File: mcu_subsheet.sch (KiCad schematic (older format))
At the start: 34 parts

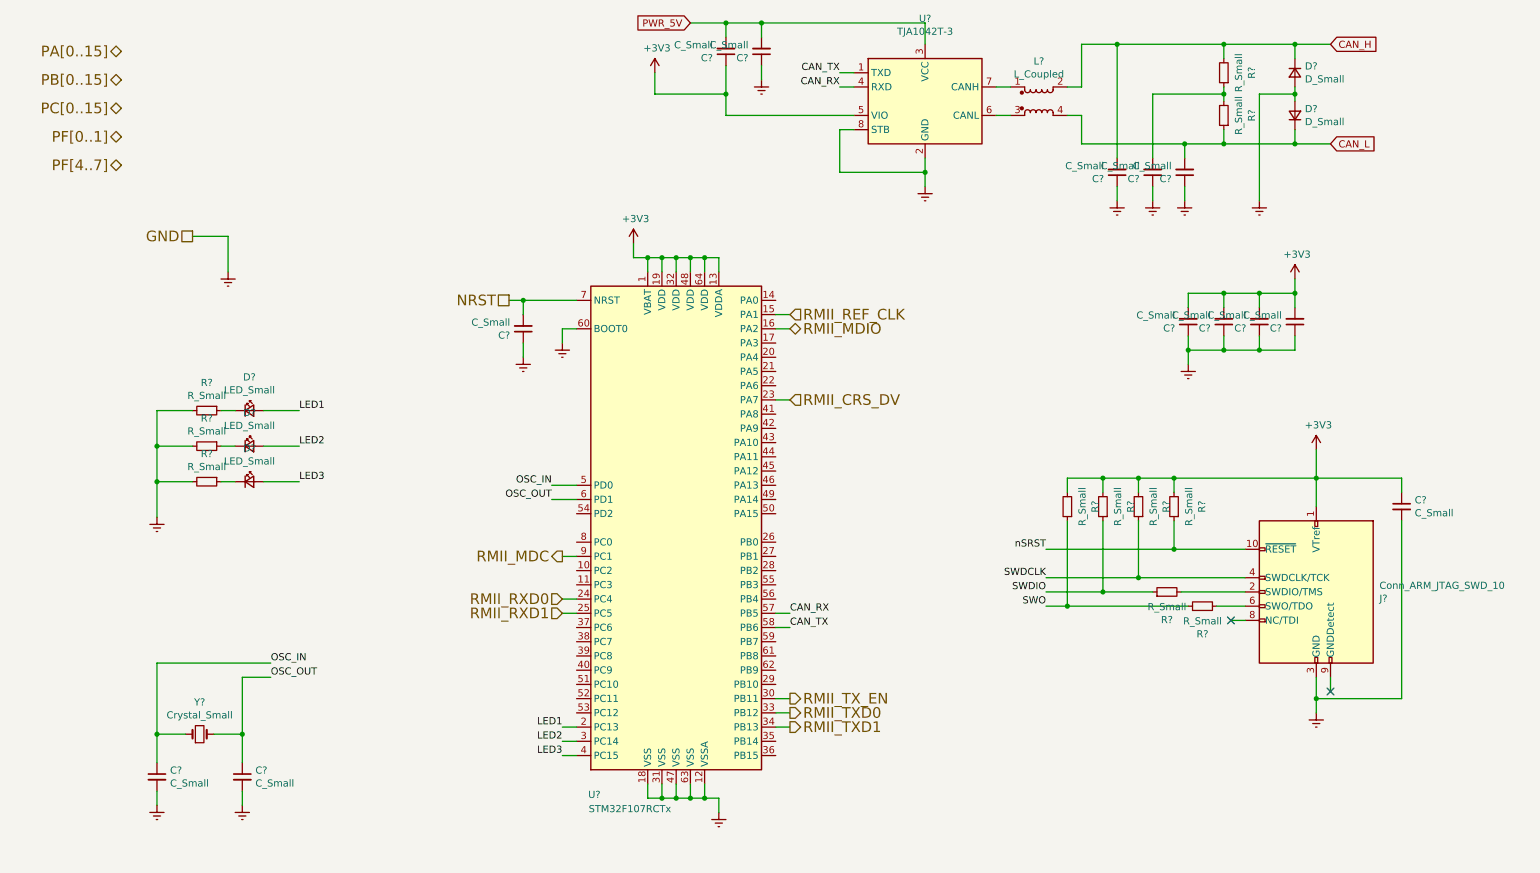
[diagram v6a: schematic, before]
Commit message: [can]:can lines protection + debug pinout connection
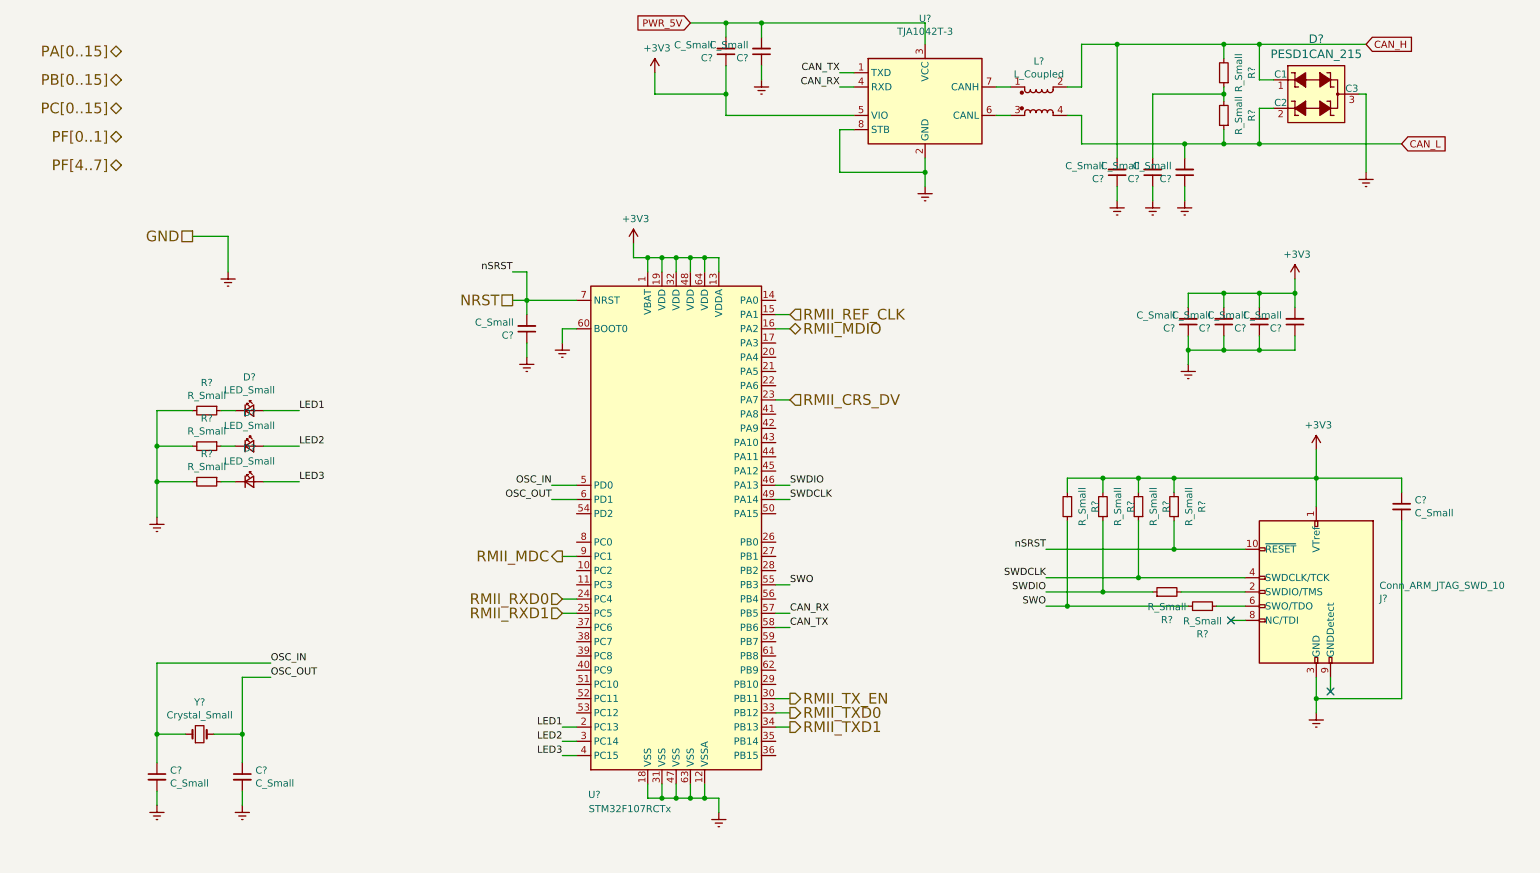
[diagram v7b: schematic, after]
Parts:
- removed D? (x2): D_Small, symbol Device:D_Small
- added D?: PESD1CAN_215, digikey-footprints:SOT-23-3, symbol dk_TVS-Diodes:PESD1CAN_215
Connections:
- net nSRST is gone; now on net NRST: J?.10 (~RESET~), R?.1
- net CAN_H: now also D?.1 (C1)
- net CAN_L: now also D?.2 (C2)
- net Earth: now also D?.3 (C3)
- net SWDCLK: now also U?.49 (PA14)
- net SWDIO: now also U?.46 (PA13)
- net SWO: now also U?.55 (PB3)
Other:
- moved on the sheet: C?
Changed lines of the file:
@@
 Text HLabel 2000 2500 0    75   UnSpc ~ 0
 GND
-Text HLabel 4225 2950 0    75   UnSpc ~ 0
+Text HLabel 4250 2950 0    75   UnSpc ~ 0
 NRST
 Text HLabel 1500 1200 0    75   BiDi ~ 0
@@
 L Device:C_Small C?
 U 1 1 61D7B19B
-P 4325 3150
-F 0 "C?" H 4417 3196 50  0000 L CNN
-F 1 "C_Small" H 4417 3105 50  0000 L CNN
-F 2 "" H 4325 3150 50  0001 C CNN
-F 3 "~" H 4325 3150 50  0001 C CNN
-	1    4325 3150
-	-1   0    0    1
-$EndComp
-Wire Wire Line
-	4325 3050 4325 2950
-Wire Wire Line
-	4325 2950 4700 2950
+P 4350 3150
+F 0 "C?" H 4442 3196 50  0000 L CNN
+F 1 "C_Small" H 4442 3105 50  0000 L CNN
+F 2 "" H 4350 3150 50  0001 C CNN
+F 3 "~" H 4350 3150 50  0001 C CNN
+	1    4350 3150
+	-1   0    0    1
+$EndComp
 $Comp
 L power:Earth #PWR?
 U 1 1 61D7EBFD
-P 4325 3350
-F 0 "#PWR?" H 4325 3100 50  0001 C CNN
-F 1 "Earth" H 4325 3200 50  0001 C CNN
-F 2 "" H 4325 3350 50  0001 C CNN
-F 3 "~" H 4325 3350 50  0001 C CNN
-	1    4325 3350
-	1    0    0    -1
-$EndComp
-Wire Wire Line
-	4325 3350 4325 3250
+P 4350 3350
+F 0 "#PWR?" H 4350 3100 50  0001 C CNN
+F 1 "Earth" H 4350 3200 50  0001 C CNN
+F 2 "" H 4350 3350 50  0001 C CNN
+F 3 "~" H 4350 3350 50  0001 C CNN
+	1    4350 3350
+	1    0    0    -1
+$EndComp
+Wire Wire Line
+	4350 3350 4350 3250
 $Comp
 L power:Earth #PWR?
@@
 Wire Wire Line
 	4600 3150 4600 3250
-Wire Wire Line
-	4225 2950 4325 2950
-Connection ~ 4325 2950
 $Comp
 L Device:Crystal_Small Y?
@@
 	1    0    0    -1
 $EndComp
-$Comp
-L Device:D_Small D?
-U 1 1 61E0E1EA
-P 9750 1350
-F 0 "D?" V 9704 1420 50  0000 L CNN
-F 1 "D_Small" V 9795 1420 50  0000 L CNN
-F 2 "" V 9750 1350 50  0001 C CNN
-F 3 "~" V 9750 1350 50  0001 C CNN
-	1    9750 1350
-	0    1    1    0
-$EndComp
-$Comp
-L Device:D_Small D?
-U 1 1 61E0EA92
-P 9750 1650
-F 0 "D?" V 9796 1580 50  0000 R CNN
-F 1 "D_Small" V 9705 1580 50  0000 R CNN
-F 2 "" V 9750 1650 50  0001 C CNN
-F 3 "~" V 9750 1650 50  0001 C CNN
-	1    9750 1650
-	0    -1   -1   0
-$EndComp
 Wire Wire Line
 	9250 1250 9250 1150
@@
 Wire Wire Line
 	8500 1150 8250 1150
-Wire Wire Line
-	9750 1250 9750 1150
 Connection ~ 9250 1150
-Wire Wire Line
-	9750 1750 9750 1850
 Connection ~ 9250 1850
 $Comp
 L power:Earth #PWR?
 U 1 1 61E219F8
-P 9500 2250
-F 0 "#PWR?" H 9500 2000 50  0001 C CNN
-F 1 "Earth" H 9500 2100 50  0001 C CNN
-F 2 "" H 9500 2250 50  0001 C CNN
-F 3 "~" H 9500 2250 50  0001 C CNN
-	1    9500 2250
-	1    0    0    -1
-$EndComp
-Text GLabel 10000 1150 2    50   Input ~ 0
+P 10250 2050
+F 0 "#PWR?" H 10250 1800 50  0001 C CNN
+F 1 "Earth" H 10250 1900 50  0001 C CNN
+F 2 "" H 10250 2050 50  0001 C CNN
+F 3 "~" H 10250 2050 50  0001 C CNN
+	1    10250 2050
+	1    0    0    -1
+$EndComp
+Text GLabel 10250 1150 2    50   Input ~ 0
 CAN_H
-Text GLabel 10000 1850 2    50   Input ~ 0
+Text GLabel 10500 1850 2    50   Input ~ 0
 CAN_L
 Wire Wire Line
-	10000 1150 9750 1150
-Wire Wire Line
-	10000 1850 9750 1850
-Wire Wire Line
-	9750 1450 9750 1500
-Connection ~ 9750 1150
-Connection ~ 9750 1850
-Wire Wire Line
-	9250 1150 9750 1150
-Wire Wire Line
-	9250 1850 9750 1850
-Wire Wire Line
-	9750 1500 9500 1500
-Wire Wire Line
-	9500 1500 9500 2250
-Connection ~ 9750 1500
-Wire Wire Line
-	9750 1500 9750 1550
+	9250 1150 9500 1150
 Wire Wire Line
 	2000 2500 2250 2500
@@
 Wire Wire Line
 	8650 4900 9400 4900
+$Comp
+L dk_TVS-Diodes:PESD1CAN_215 D?
+U 1 1 61EEEF3D
+P 9900 1500
+F 0 "D?" H 9900 1887 60  0000 C CNN
+F 1 "PESD1CAN_215" H 9900 1781 60  0000 C CNN
+F 2 "digikey-footprints:SOT-23-3" H 10100 1700 60  0001 L CNN
+F 3 "https://assets.nexperia.com/documents/data-sheet/PESD1CAN.pdf" H 10100 1800 60  0001 L CNN
+F 4 "1727-3817-1-ND" H 10100 1900 60  0001 L CNN "Digi-Key_PN"
+F 5 "PESD1CAN,215" H 10100 2000 60  0001 L CNN "MPN"
+F 6 "Circuit Protection" H 10100 2100 60  0001 L CNN "Category"
+F 7 "TVS - Diodes" H 10100 2200 60  0001 L CNN "Family"
+F 8 "https://assets.nexperia.com/documents/data-sheet/PESD1CAN.pdf" H 10100 2300 60  0001 L CNN "DK_Datasheet_Link"
+F 9 "/product-detail/en/nexperia-usa-inc/PESD1CAN,215/1727-3817-1-ND/1530822" H 10100 2400 60  0001 L CNN "DK_Detail_Page"
+F 10 "TVS DIODE 24V 70V SOT23" H 10100 2500 60  0001 L CNN "Description"
+F 11 "Nexperia USA Inc." H 10100 2600 60  0001 L CNN "Manufacturer"
+F 12 "Active" H 10100 2700 60  0001 L CNN "Status"
+	1    9900 1500
+	1    0    0    -1
+$EndComp
+Wire Wire Line
+	9600 1400 9500 1400
+Wire Wire Line
+	9500 1400 9500 1150
+Connection ~ 9500 1150
+Wire Wire Line
+	9500 1150 10250 1150
+Wire Wire Line
+	9250 1850 9500 1850
+Wire Wire Line
+	9600 1600 9500 1600
+Wire Wire Line
+	9500 1600 9500 1850
+Wire Wire Line
+	10200 1500 10250 1500
+Wire Wire Line
+	10250 1500 10250 2050
+Wire Wire Line
+	9500 1850 10500 1850
+Connection ~ 9500 1850
+Wire Wire Line
+	6100 4250 6200 4250
+Text Label 6200 4250 0    50   ~ 0
+SWDIO
+Text Label 6200 4350 0    50   ~ 0
+SWDCLK
+Wire Wire Line
+	6200 4350 6100 4350
+Text Label 4250 2750 2    50   ~ 0
+nSRST
+Wire Wire Line
+	4350 2750 4350 2950
+Wire Wire Line
+	4250 2750 4350 2750
+Wire Wire Line
+	4250 2950 4350 2950
+Wire Wire Line
+	4350 2950 4700 2950
+Connection ~ 4350 2950
+Wire Wire Line
+	4350 2950 4350 3050
+Text Label 6200 4950 0    50   ~ 0
+SWO
+Wire Wire Line
+	6200 4950 6100 4950
 $EndSCHEMATC
